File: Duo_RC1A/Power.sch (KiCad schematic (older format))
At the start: 29 parts, among them U2 MC7805, U3 NCP1117DT33G

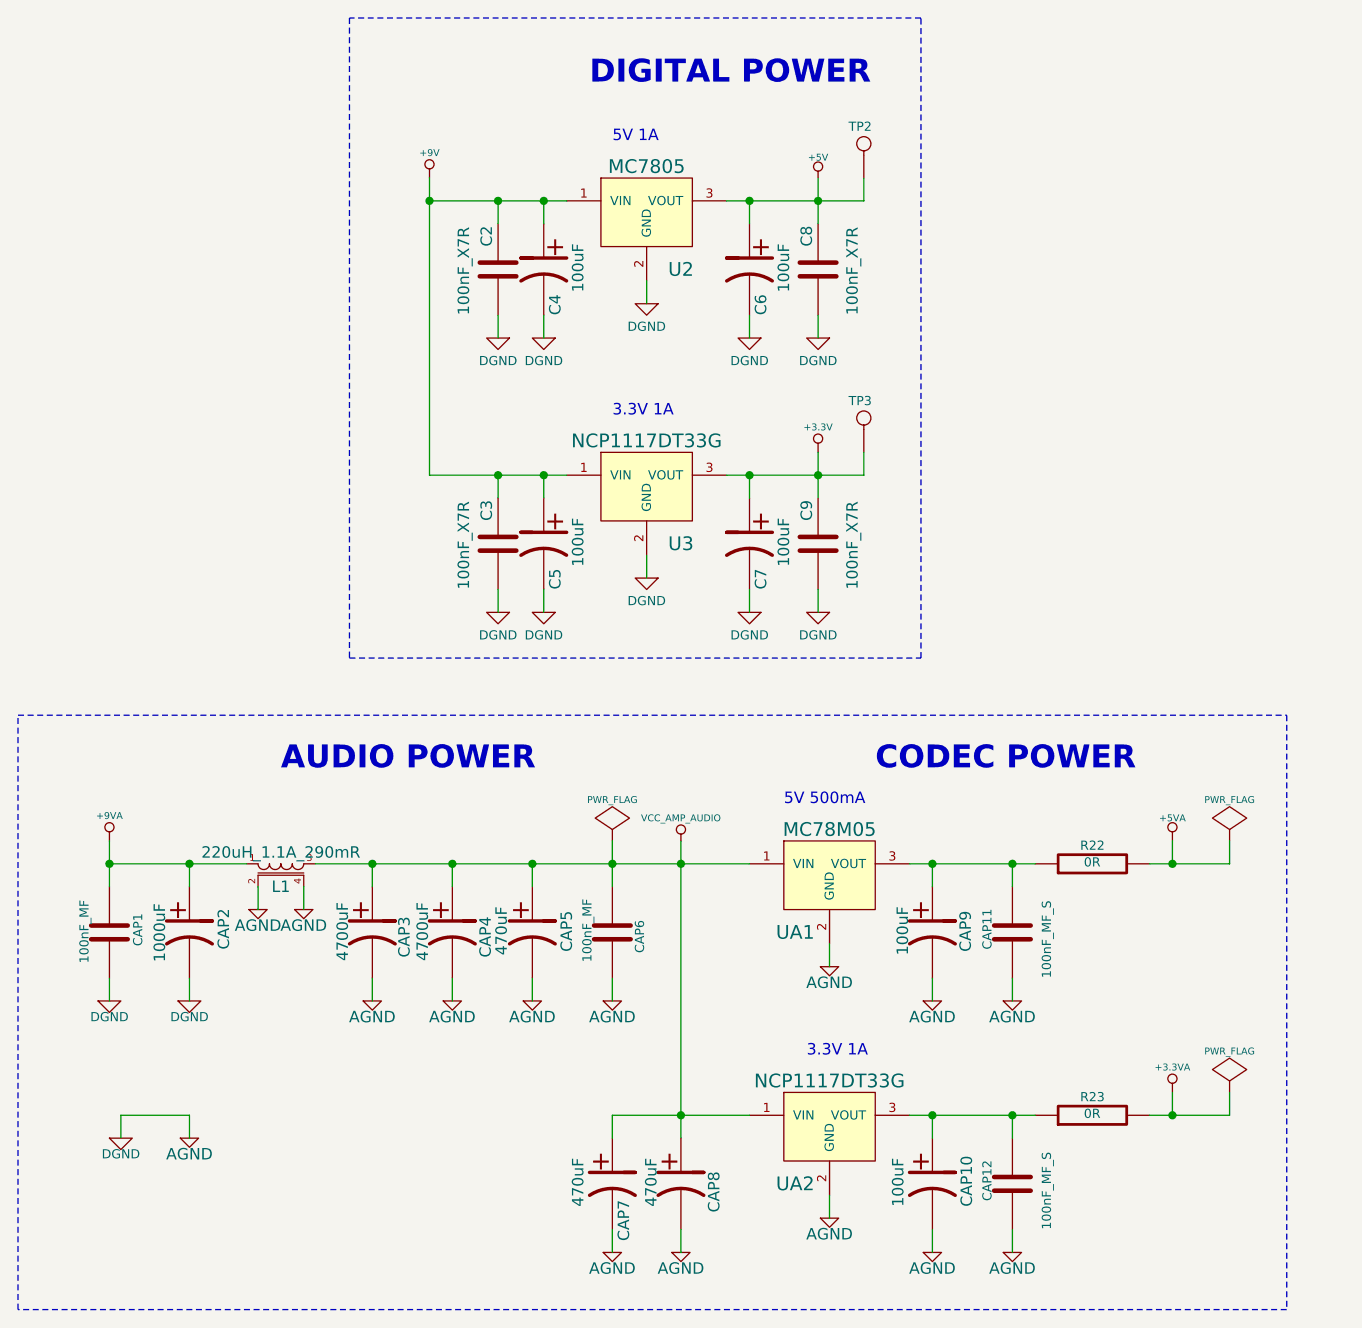
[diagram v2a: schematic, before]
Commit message: Rear pannel layout finished. First layout of sound modules.
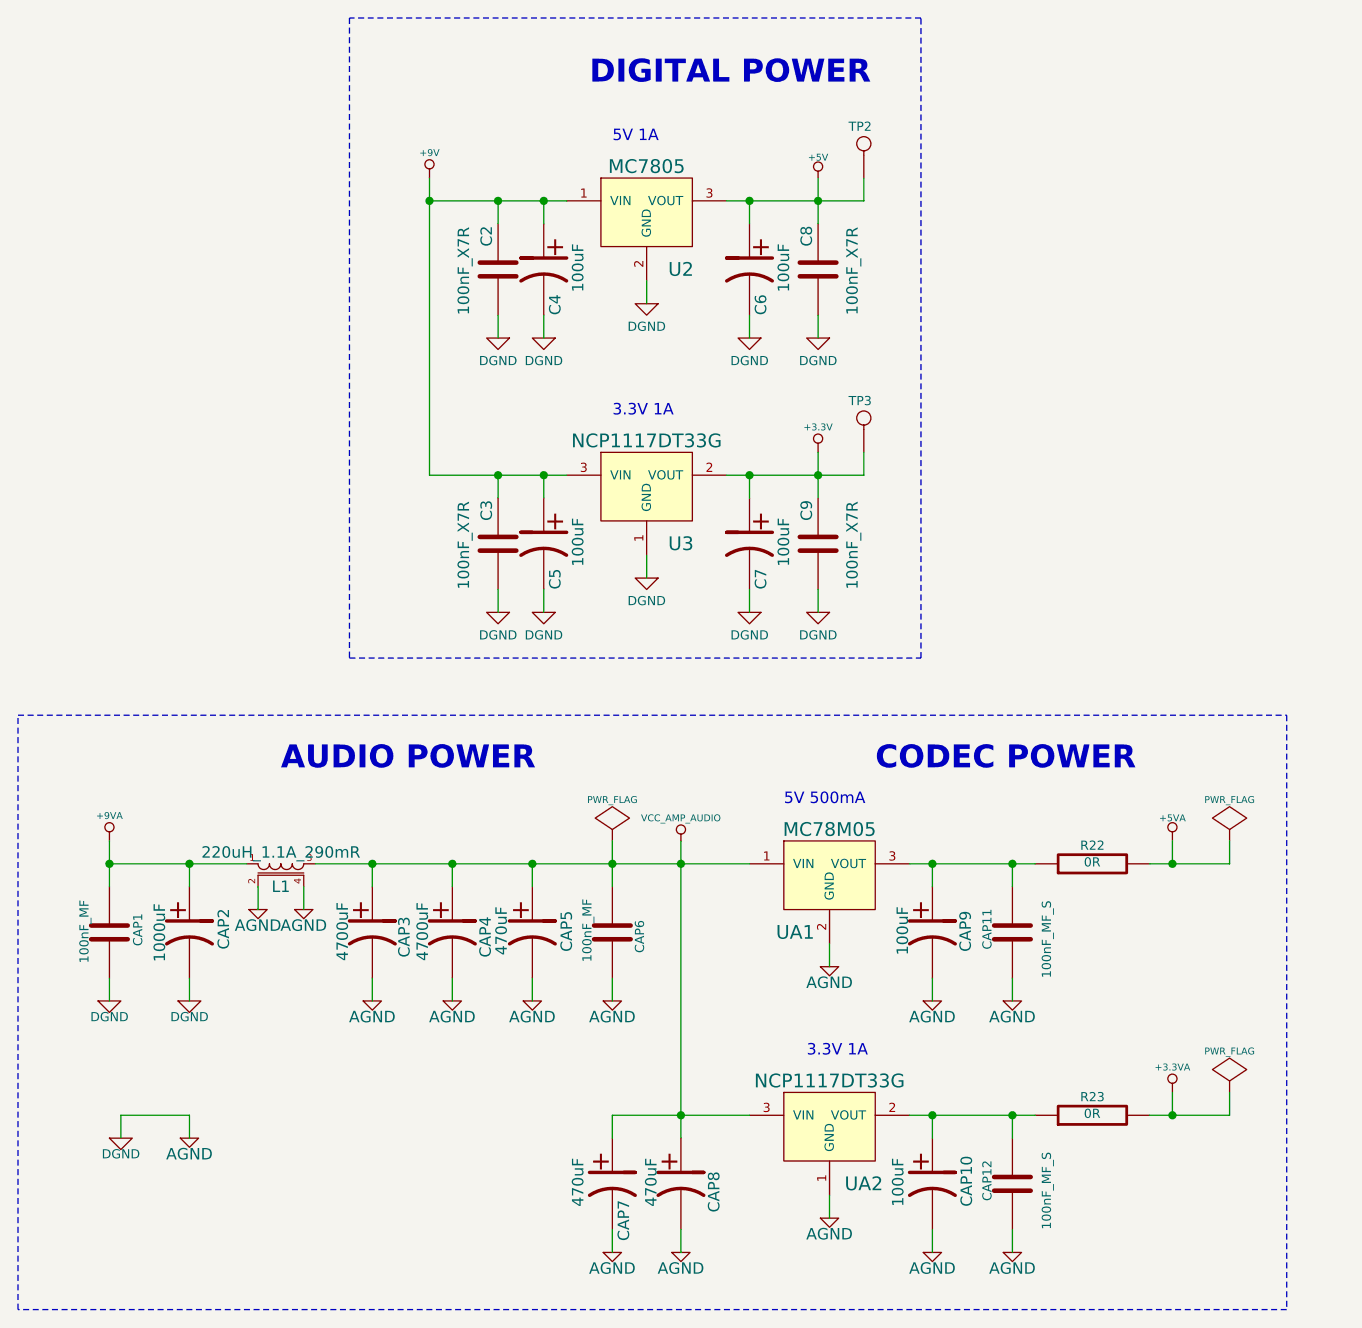
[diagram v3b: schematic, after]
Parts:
- removed U3, UA2: NCP1117DT33G, Duo_Audio_HMI_RC1A:DPAK(369C), symbol LINEAR_REGULATOR_DPAK_3P
- added U3, UA2: NCP1117DT33G, Duo_Audio_HMI_RC1A:DPAK(369C), symbol NCP1117DT33G
- CAP5: footprint Duo_Audio_HMI_RC1A:Capacitor10x21RM5 -> Duo_Audio_HMI_RC1A:Capacitor8x13RM3.5
- TP3: footprint Duo_Audio_HMI_RC1A:TESTPOINT_1MM -> Duo_Audio_HMI_RC1A:TESTPOINT_2.2MM
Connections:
- net +3.3V: now also U3.2 (VOUT)
- net +9V: now also U3.3 (VIN)
- net AGND: now also U3.1 (GND), UA2.1 (GND)
- net VCC_AMP_AUDIO: now also UA2.3 (VIN)
- net at CAP10.1, CAP12.1, R23.1: now also UA2.2 (VOUT)
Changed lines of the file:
@@
 F 0 "CAP5" V 5250 4665 50  0000 L CNN
 F 1 "470uF" V 4965 4650 50  0000 L CNN
-F 2 "Duo_Audio_HMI_RC1A:Capacitor10x21RM5" H 5100 4750 60  0001 C CNN
+F 2 "Duo_Audio_HMI_RC1A:Capacitor8x13RM3.5" H 5100 4750 60  0001 C CNN
 F 3 "~" H 5100 4750 60  0000 C CNN
 	1    5100 4750
@@
 CODEC POWER
 $Comp
-L LINEAR_REGULATOR_DPAK_3P UA2
-U 1 1 537BBEBD
-P 6400 5600
-F 0 "UA2" H 6250 5350 60  0000 C CNN
-F 1 "NCP1117DT33G" H 6400 5800 60  0000 C CNN
-F 2 "Duo_Audio_HMI_RC1A:DPAK(369C)" H 6400 5650 60  0001 C CNN
-F 3 "~" H 6400 5650 60  0000 C CNN
-	1    6400 5600
-	1    0    0    -1
-$EndComp
-$Comp
 L +9V #PWR038
 U 1 1 537BBEC2
@@
 F 3 "~" H 5600 1650 60  0000 C CNN
 	1    5600 1600
-	1    0    0    -1
-$EndComp
-$Comp
-L LINEAR_REGULATOR_DPAK_3P U3
-U 1 1 537BBEE1
-P 5600 2800
-F 0 "U3" H 5750 2550 60  0000 C CNN
-F 1 "NCP1117DT33G" H 5600 3000 60  0000 C CNN
-F 2 "Duo_Audio_HMI_RC1A:DPAK(369C)" H 5600 2850 60  0001 C CNN
-F 3 "~" H 5600 2850 60  0000 C CNN
-	1    5600 2800
 	1    0    0    -1
 $EndComp
@@
 F 0 "TP3" V 6625 2465 40  0000 L CNN
 F 1 "TEST_POINT_1MM" H 6550 2555 30  0001 C CNN
-F 2 "Duo_Audio_HMI_RC1A:TESTPOINT_1MM" H 6550 2500 60  0001 C CNN
+F 2 "Duo_Audio_HMI_RC1A:TESTPOINT_2.2MM" H 6550 2500 60  0001 C CNN
 F 3 "" H 6550 2500 60  0000 C CNN
 	1    6550 2500
@@
 Wire Wire Line
 	5150 1550 5150 1650
+$Comp
+L NCP1117DT33G U3
+U 1 1 53849D6A
+P 5600 2800
+F 0 "U3" H 5750 2550 60  0000 C CNN
+F 1 "NCP1117DT33G" H 5600 3000 60  0000 C CNN
+F 2 "Duo_Audio_HMI_RC1A:DPAK(369C)" H 5600 2850 60  0001 C CNN
+F 3 "" H 5600 2850 60  0000 C CNN
+	1    5600 2800
+	1    0    0    -1
+$EndComp
+$Comp
+L NCP1117DT33G UA2
+U 1 1 53849DCD
+P 6400 5600
+F 0 "UA2" H 6550 5350 60  0000 C CNN
+F 1 "NCP1117DT33G" H 6400 5800 60  0000 C CNN
+F 2 "Duo_Audio_HMI_RC1A:DPAK(369C)" H 6400 5650 60  0001 C CNN
+F 3 "" H 6400 5650 60  0000 C CNN
+	1    6400 5600
+	1    0    0    -1
+$EndComp
 $EndSCHEMATC

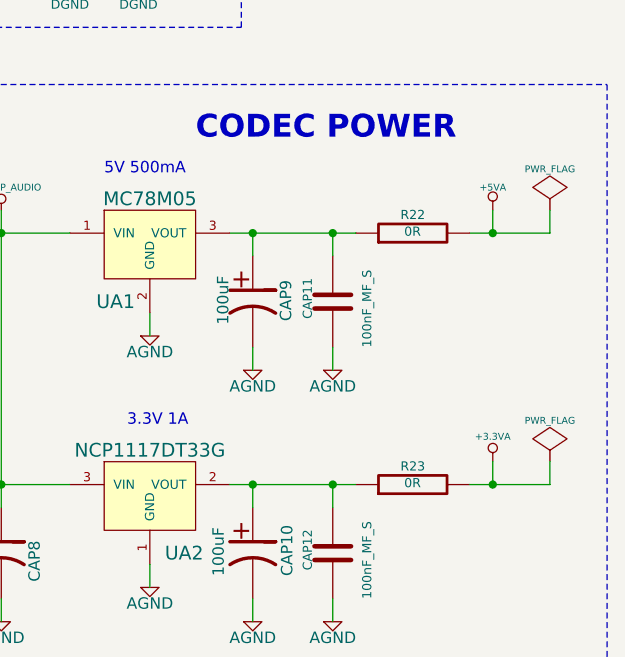
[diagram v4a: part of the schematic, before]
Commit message: Schematic for BOM for ITEAD quote. BottomBoard initial audio placement. Needs to change the ground cuts and the Audio VCC (9V) path.
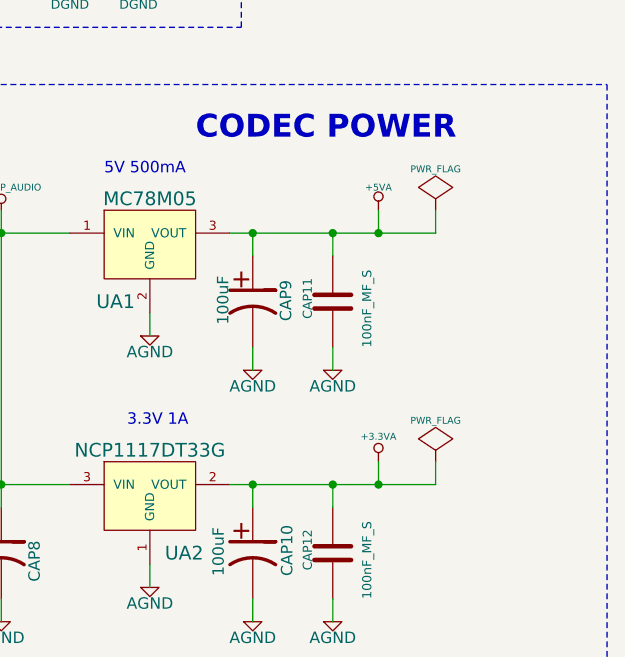
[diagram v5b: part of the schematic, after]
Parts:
- removed R22, R23: 0R, Duo_Audio_HMI_RC1A:SM0805, symbol R
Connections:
- net +3.3VA: now also CAP10.1, CAP12.1, UA2.2 (VOUT)
- net +5VA: now also CAP11.1, CAP9.1, UA1.3 (VOUT)

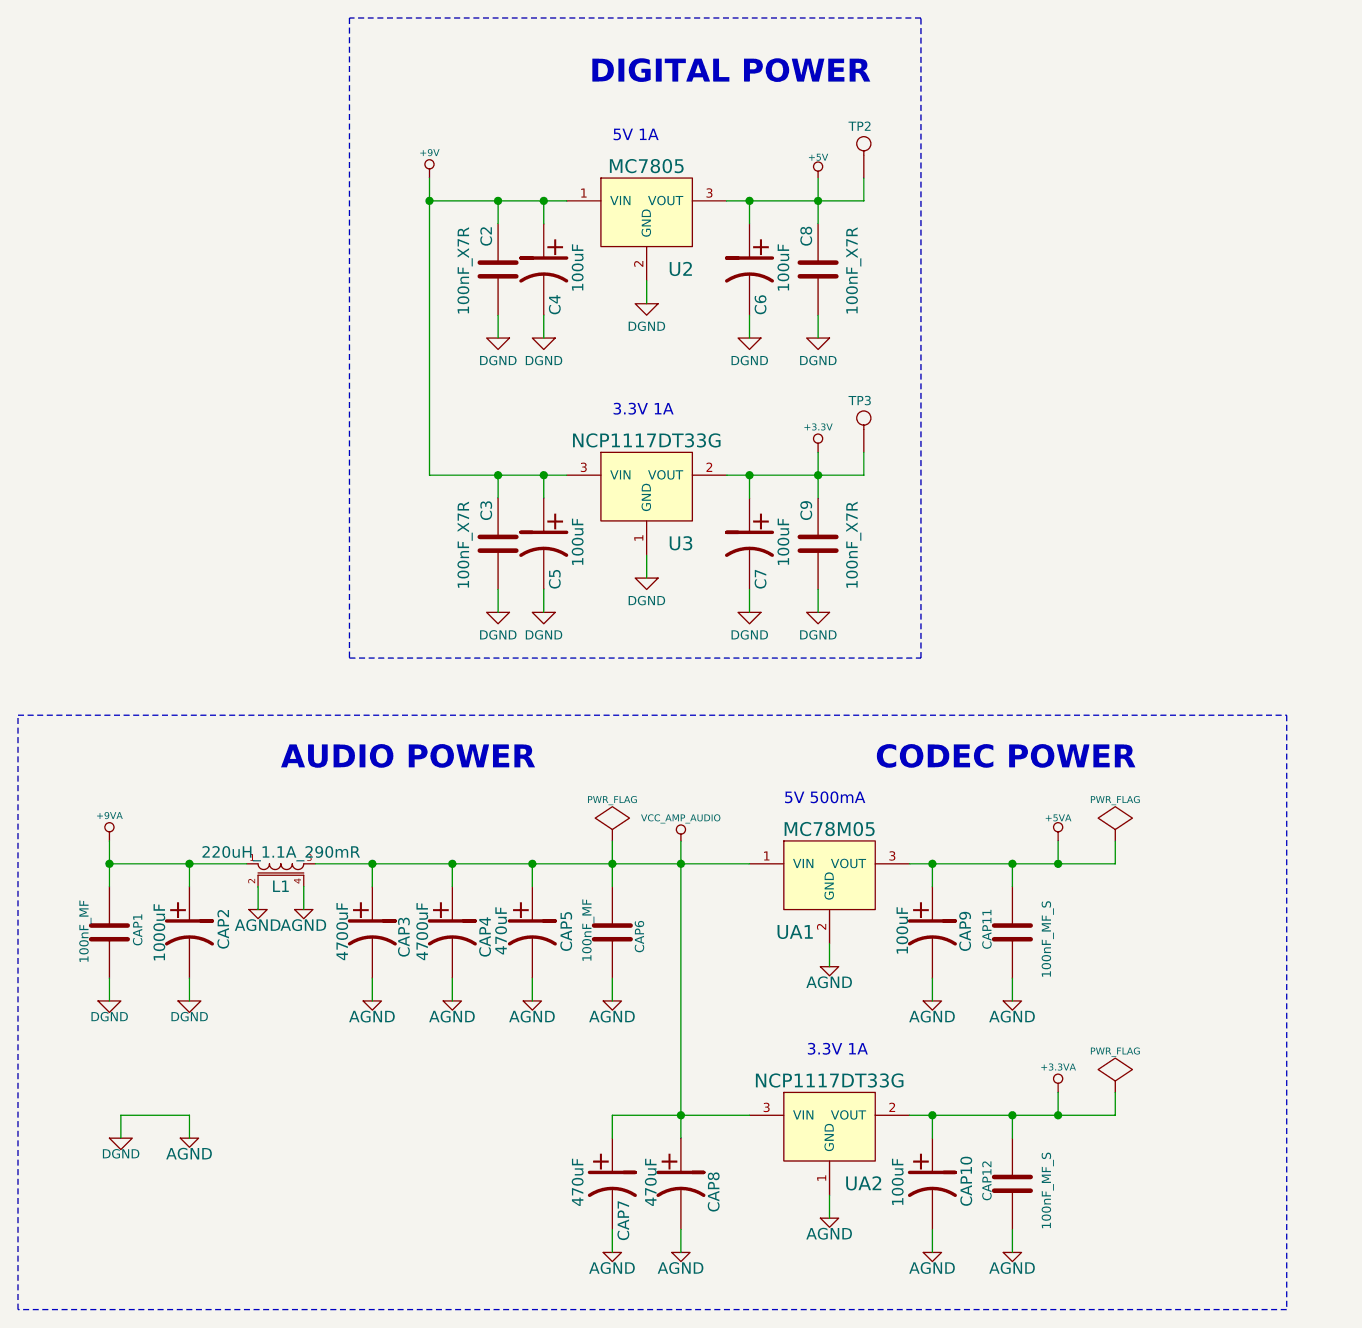
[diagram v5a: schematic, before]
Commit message: Changed the LCD for the 2.8pol. Rotated the bottom board connector. Moved the 3.3V linear regulator from the bottom board to the top board, and changed the power for the top board from 3.3V to 9V.
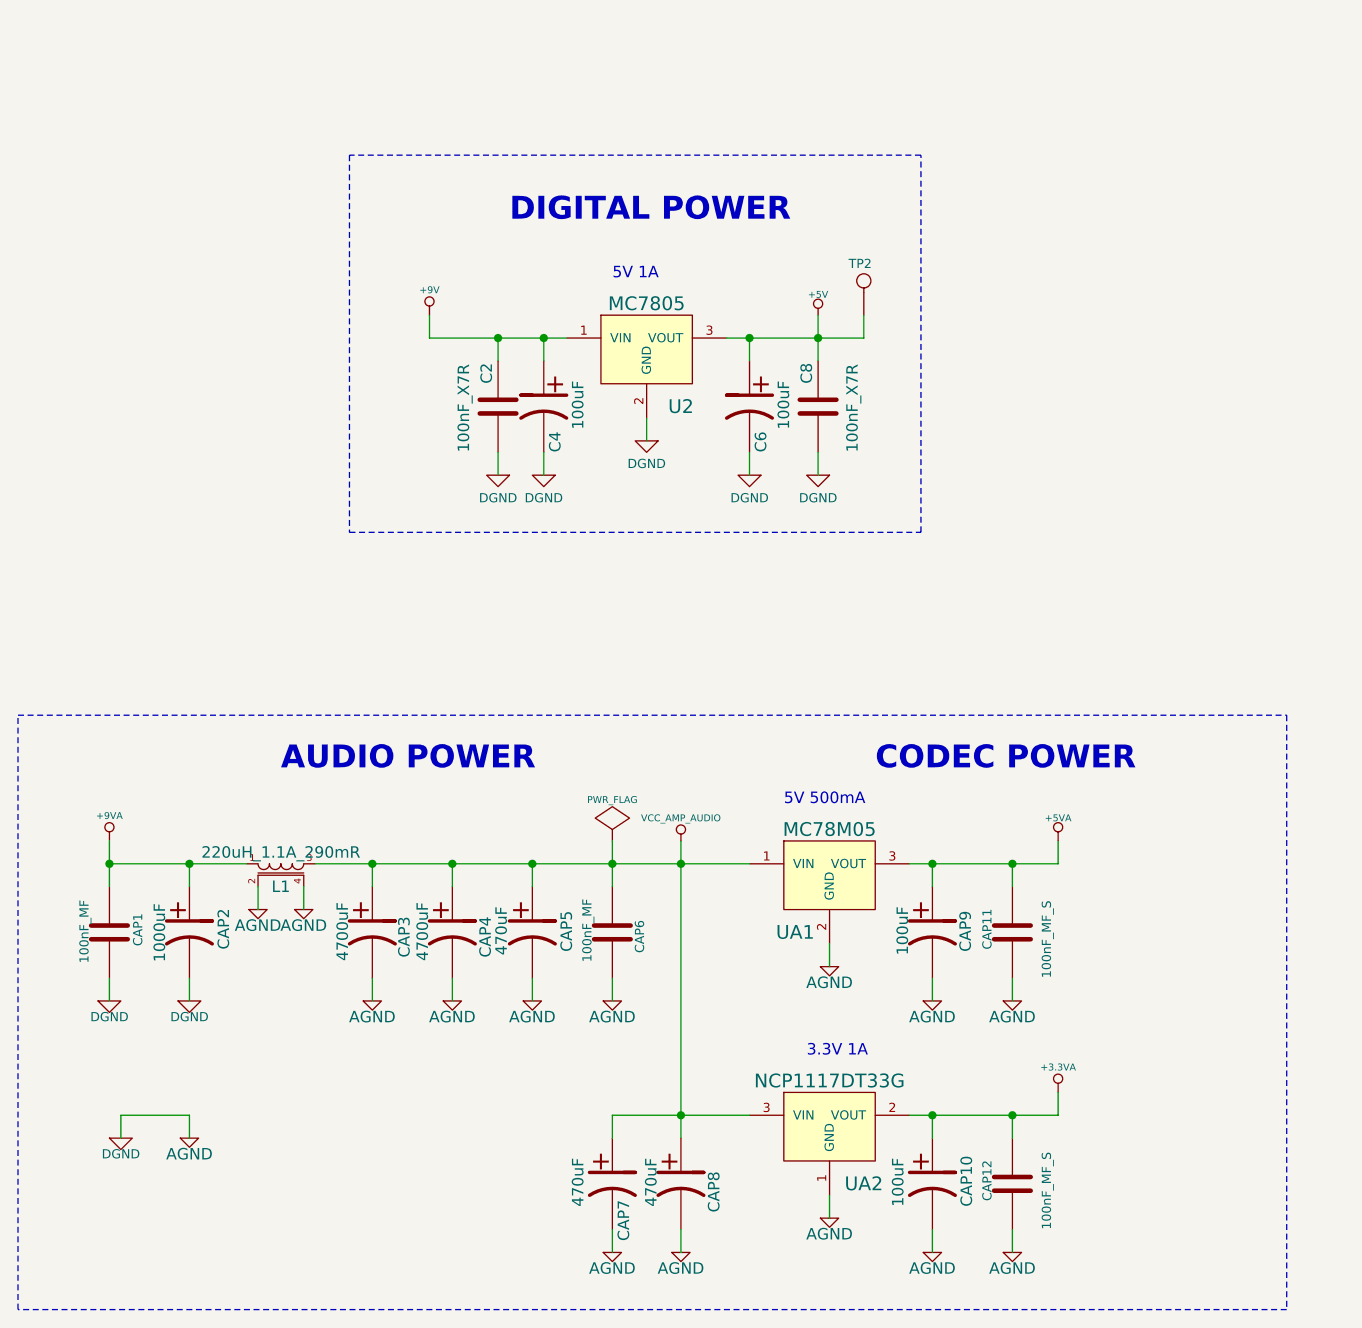
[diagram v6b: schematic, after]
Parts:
- removed C3, C9: 100nF_X7R, Duo_Audio_HMI_RC1A:SM0603, symbol C
- removed C5, C7: 100uF, Duo_Audio_HMI_RC1A:Capacitor5x11RM2, symbol CP1
- removed TP3: TEST_POINT_1MM, Duo_Audio_HMI_RC1A:TESTPOINT_2.2MM, symbol CONN_1
- removed U3: NCP1117DT33G, Duo_Audio_HMI_RC1A:DPAK(369C), symbol NCP1117DT33G
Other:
- moved on the sheet: C2, C4, C6, C8, TP2, U2
